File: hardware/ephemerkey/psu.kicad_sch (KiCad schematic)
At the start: 24 parts, among them J3 USB-C, J4 BAT 1S Li-ion, J5 USB-C (vert), Q1 AO3401A, U2 TPS63900DSKR, U3 USBLC6-2SC6, U4 MCP73831-2-OT

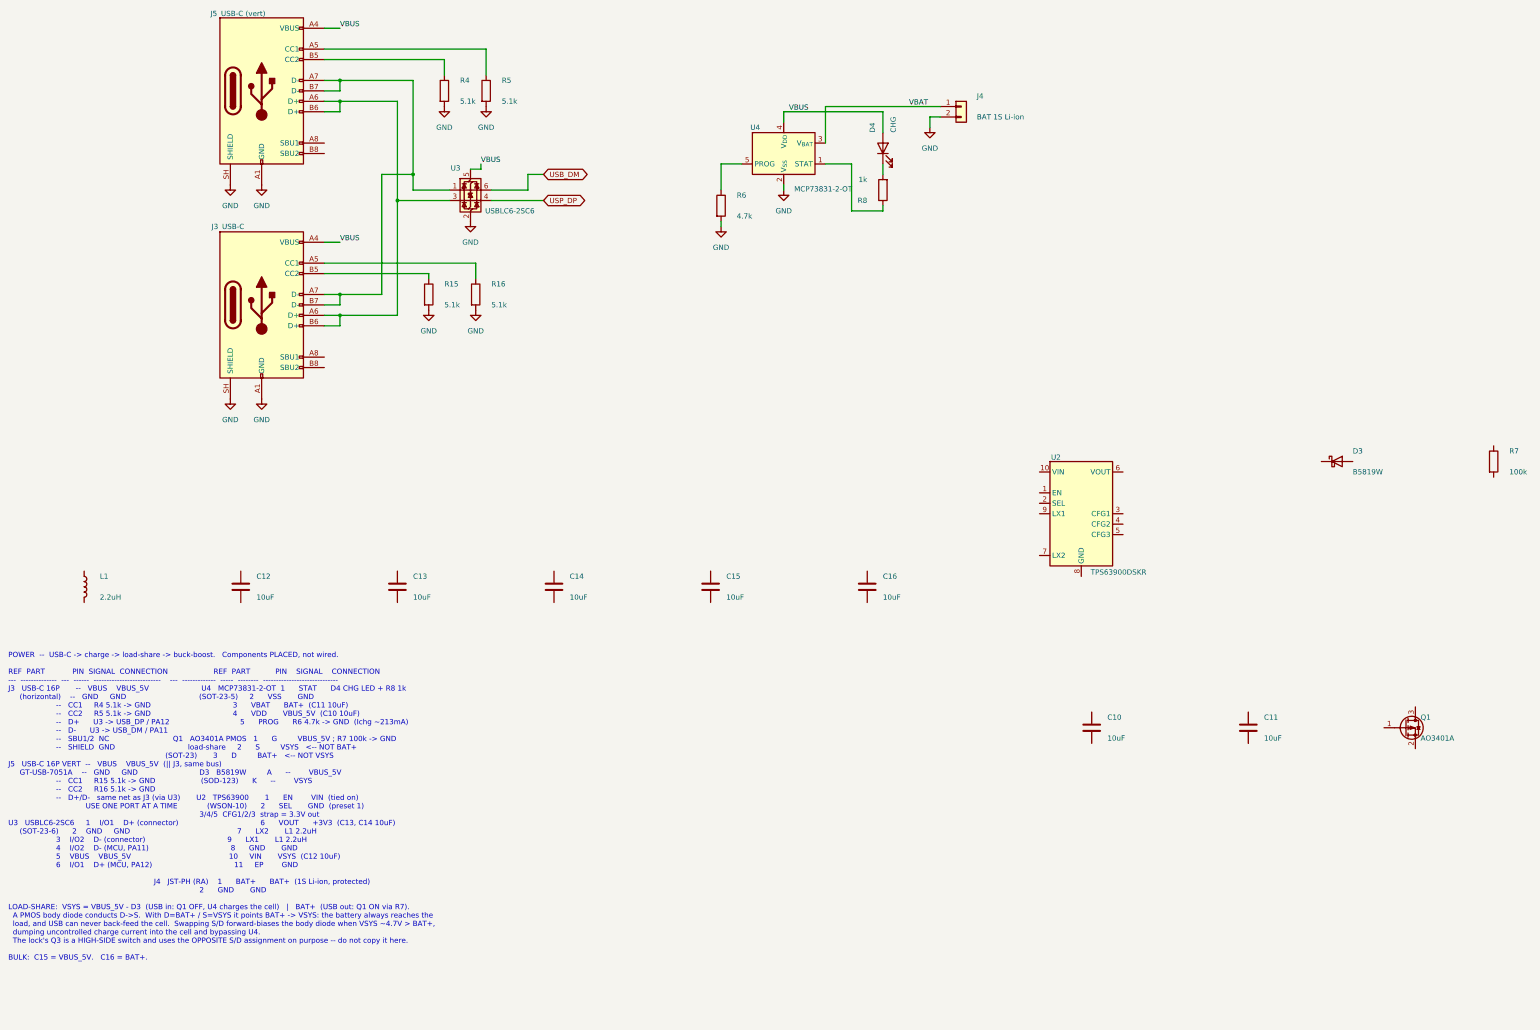
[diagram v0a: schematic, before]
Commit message: hardware: add TPS63900 R2D CFG straps (R27-R29) to psu sheet + PARTS.md
Reflect the CFG1/2/3 strap resistors (already in the schgen manifest) in the
psu.kicad_sch placement + note, and document them in PARTS.md (R27 36.5k, R28
0R, R29 16.2k; 1% for the R2D interface, both presets 3.3V, I_lim unlimited).
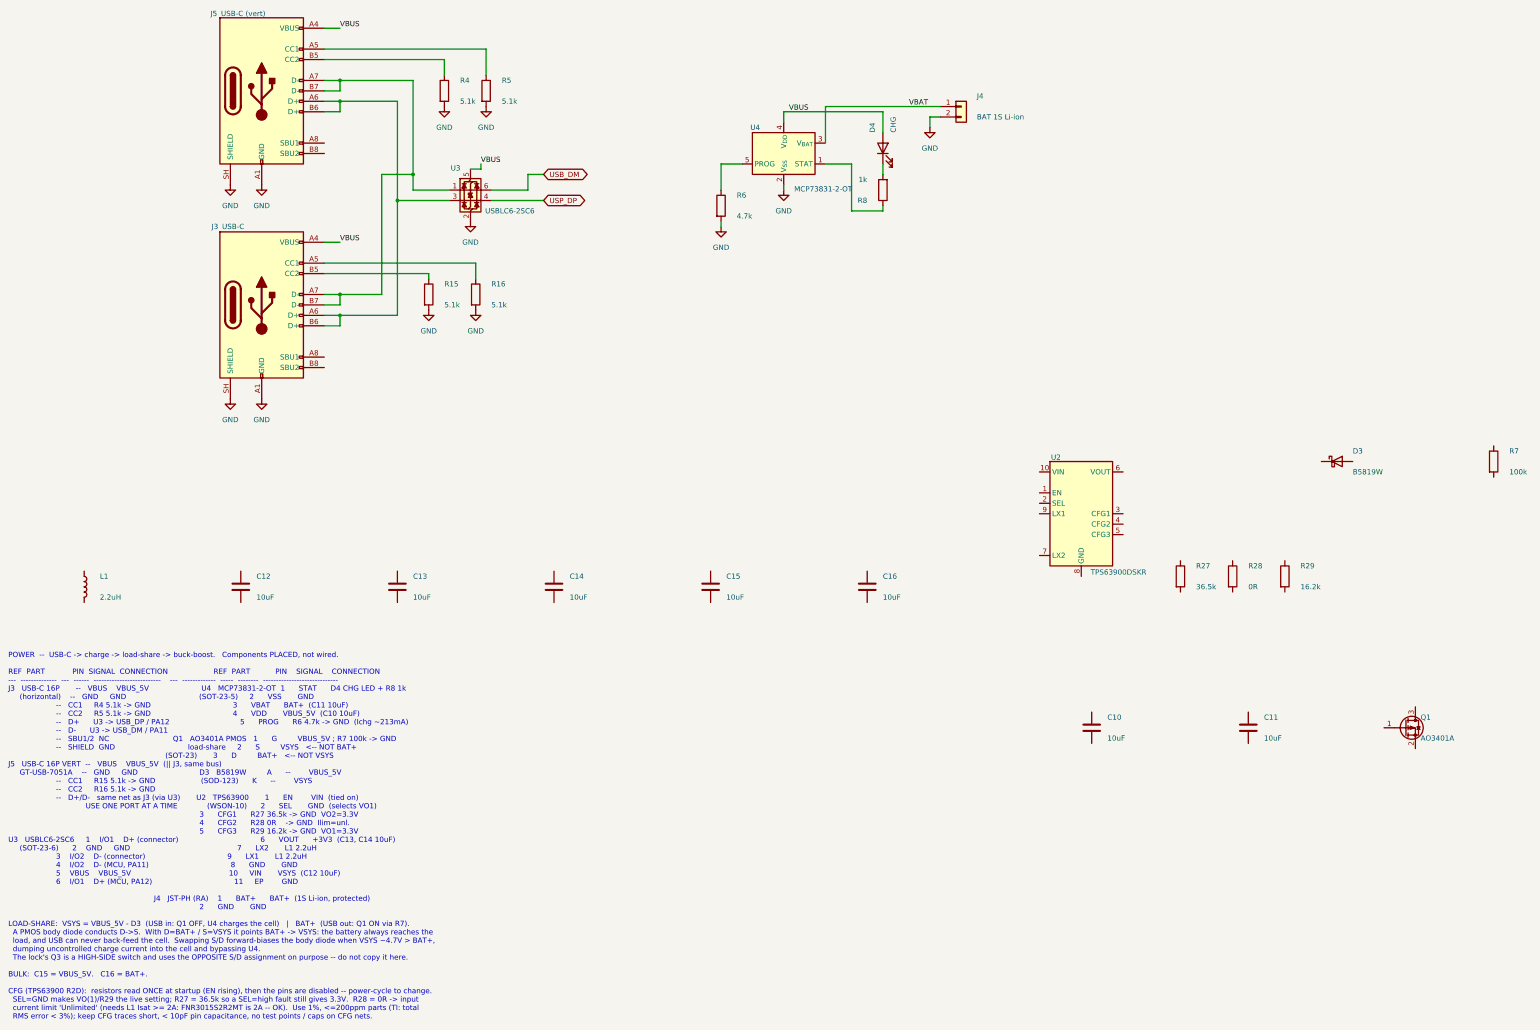
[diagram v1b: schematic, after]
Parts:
- added R27: 36.5k, Resistor_SMD:R_0402_1005Metric, symbol Device:R
- added R28: 0R, Resistor_SMD:R_0402_1005Metric, symbol Device:R
- added R29: 16.2k, Resistor_SMD:R_0402_1005Metric, symbol Device:R
